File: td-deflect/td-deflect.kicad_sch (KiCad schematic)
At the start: 83 parts, among them J10 Conn_01x02_Male, J11 Conn_01x02_Male, Q1 BSZ42DN25NS3GATMA1, Q10 IPD50R380CE, Q11 IPD50R380CE, Q2 G3R450MT17D, Q3 BSZ42DN25NS3GATMA1, Q4 BCP56, Q5 BCP53, Q6 BD139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

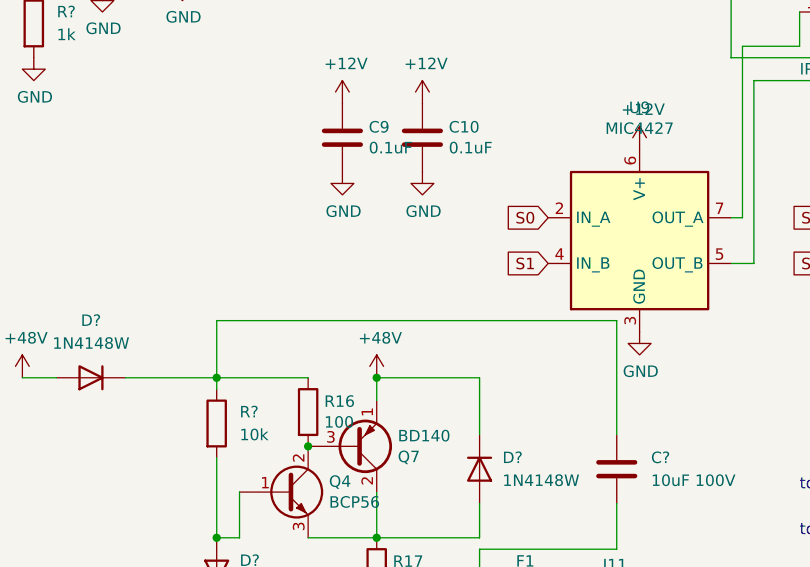
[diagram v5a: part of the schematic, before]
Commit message: make bootstrap circuit not bootstrap as much
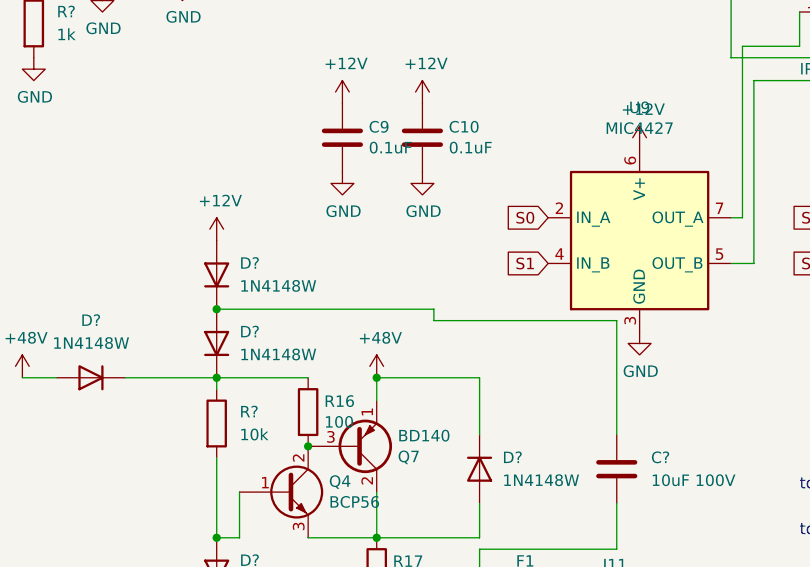
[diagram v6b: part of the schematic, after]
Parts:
- added D? (x2): 1N4148W, Diode_SMD:D_SOD-123, symbol Diode:1N4148W
- C5, C7: Digikey 1276-1099-1-ND -> (none); Voltage 10V -> 50V
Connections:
- net +12V: now also D?.2 (A)
- net at D?.1 (K), R16.1, R?.1: now also D?.1 (K); no longer C?.1
- new net: C?.1, D?.1 (K), D?.2 (A)
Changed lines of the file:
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@@
   (junction (at 214.63 93.98) (diameter 1.016) (color 0 0 0 0)
   )
+  (junction (at 128.27 121.92) (diameter 0) (color 0 0 0 0)
+  )
   (junction (at 71.12 45.72) (diameter 0) (color 0 0 0 0)
   )
@@
     (stroke (width 0) (type default) (color 0 0 0 0))
   )
-  (wire (pts (xy 172.72 123.19) (xy 128.27 123.19))
-    (stroke (width 0) (type default) (color 0 0 0 0))
-  )
   (wire (pts (xy 17.78 166.37) (xy 17.78 168.91))
     (stroke (width 0) (type solid) (color 0 0 0 0))
@@
     (stroke (width 0) (type solid) (color 0 0 0 0))
   )
-  (wire (pts (xy 128.27 123.19) (xy 128.27 129.54))
-    (stroke (width 0) (type default) (color 0 0 0 0))
-  )
   (wire (pts (xy 204.47 93.98) (xy 214.63 93.98))
     (stroke (width 0) (type solid) (color 0 0 0 0))
@@
     (stroke (width 0) (type solid) (color 0 0 0 0))
   )
+  (wire (pts (xy 152.4 123.19) (xy 172.72 123.19))
+    (stroke (width 0) (type default) (color 0 0 0 0))
+  )
   (wire (pts (xy 228.6 83.82) (xy 232.41 83.82))
     (stroke (width 0) (type solid) (color 0 0 0 0))
@@
     (stroke (width 0) (type default) (color 0 0 0 0))
   )
+  (wire (pts (xy 152.4 121.92) (xy 152.4 123.19))
+    (stroke (width 0) (type default) (color 0 0 0 0))
+  )
   (wire (pts (xy 71.12 33.02) (xy 68.58 33.02))
     (stroke (width 0) (type solid) (color 0 0 0 0))
@@
     (stroke (width 0) (type solid) (color 0 0 0 0))
   )
+  (wire (pts (xy 128.27 121.92) (xy 152.4 121.92))
+    (stroke (width 0) (type default) (color 0 0 0 0))
+  )
   (wire (pts (xy 246.38 83.82) (xy 246.38 85.09))
     (stroke (width 0) (type solid) (color 0 0 0 0))
@@
       (effects (font (size 1.27 1.27)) hide)
     )
-    (property "Voltage" "10V" (id 4) (at 77.47 129.54 0)
+    (property "Voltage" "50V" (id 4) (at 77.47 129.54 0)
       (effects (font (size 1.27 1.27)) hide)
     )
-    (property "Digikey" "1276-1099-1-ND" (id 5) (at 77.47 129.54 0)
+    (property "Digikey" "" (id 5) (at 77.47 129.54 0)
       (effects (font (size 1.27 1.27)) hide)
     )
@@
       (effects (font (size 1.27 1.27)) hide)
     )
-    (property "Voltage" "10V" (id 4) (at 90.17 130.81 0)
+    (property "Voltage" "50V" (id 4) (at 90.17 130.81 0)
       (effects (font (size 1.27 1.27)) hide)
     )
-    (property "Digikey" "1276-1099-1-ND" (id 5) (at 90.17 130.81 0)
+    (property "Digikey" "" (id 5) (at 90.17 130.81 0)
       (effects (font (size 1.27 1.27)) hide)
     )
@@
     (pin "4")
   )
+  (symbol (lib_id "power:+12V") (at 128.27 114.3 0) (unit 1)
+    (in_bom yes) (on_board yes)
+    (property "Reference" "#PWR?" (id 0) (at 128.27 118.11 0)
+      (effects (font (size 1.27 1.27)) hide)
+    )
+    (property "Value" "+12V" (id 1) (at 128.651 109.9058 0))
+    (property "Footprint" "" (id 2) (at 128.27 114.3 0)
+      (effects (font (size 1.27 1.27)) hide)
+    )
+    (property "Datasheet" "" (id 3) (at 128.27 114.3 0)
+      (effects (font (size 1.27 1.27)) hide)
+    )
+    (pin "1")
+  )
   (symbol (lib_id "power:GND") (at 107.95 93.98 0) (unit 1)
     (in_bom yes) (on_board yes)
@@
     (pin "2")
   )
+  (symbol (lib_id "Diode:1N4148W") (at 128.27 118.11 90) (unit 1)
+    (in_bom yes) (on_board yes) (fields_autoplaced)
+    (property "Reference" "D?" (id 0) (at 130.81 116.8399 90)
+      (effects (font (size 1.27 1.27)) (justify right))
+    )
+    (property "Value" "1N4148W" (id 1) (at 130.81 119.3799 90)
+      (effects (font (size 1.27 1.27)) (justify right))
+    )
+    (property "Footprint" "Diode_SMD:D_SOD-123" (id 2) (at 132.715 118.11 0)
+      (effects (font (size 1.27 1.27)) hide)
+    )
+    (property "Datasheet" "https://www.vishay.com/docs/85748/1n4148w.pdf" (id 3) (at 128.27 118.11 0)
+      (effects (font (size 1.27 1.27)) hide)
+    )
+    (pin "1")
+    (pin "2")
+  )
   (symbol (lib_id "Diode:1N4148W") (at 157.48 139.7 270) (unit 1)
     (in_bom yes) (on_board yes) (fields_autoplaced)
@@
     (pin "1")
   )
+  (symbol (lib_id "Diode:1N4148W") (at 128.27 125.73 90) (unit 1)
+    (in_bom yes) (on_board yes) (fields_autoplaced)
+    (property "Reference" "D?" (id 0) (at 130.81 124.4599 90)
+      (effects (font (size 1.27 1.27)) (justify right))
+    )
+    (property "Value" "1N4148W" (id 1) (at 130.81 126.9999 90)
+      (effects (font (size 1.27 1.27)) (justify right))
+    )
+    (property "Footprint" "Diode_SMD:D_SOD-123" (id 2) (at 132.715 125.73 0)
+      (effects (font (size 1.27 1.27)) hide)
+    )
+    (property "Datasheet" "https://www.vishay.com/docs/85748/1n4148w.pdf" (id 3) (at 128.27 125.73 0)
+      (effects (font (size 1.27 1.27)) hide)
+    )
+    (pin "1")
+    (pin "2")
+  )
   (symbol (lib_id "Device:R") (at 107.95 90.17 0) (unit 1)
     (in_bom yes) (on_board yes) (fields_autoplaced)
@@
       (reference "#PWR?") (unit 1) (value "-12V") (footprint "")
     )
+    (path "/5b7a1bb3-24df-4abf-84ba-0b9034b3a7c4"
+      (reference "#PWR?") (unit 1) (value "+12V") (footprint "")
+    )
     (path "/00000000-0000-0000-0000-00005d9d9196/5eaa695f-59c3-45de-9623-f11dde8baf91"
       (reference "#PWR?") (unit 1) (value "GND") (footprint "")
@@
       (reference "D?") (unit 1) (value "1N4148W") (footprint "Diode_SMD:D_SOD-123")
     )
+    (path "/9f6b373c-73ae-40b1-af0e-5857c91d4112"
+      (reference "D?") (unit 1) (value "1N4148W") (footprint "Diode_SMD:D_SOD-123")
+    )
     (path "/b5b4e66c-1245-4e6f-b506-9e842e977f02"
       (reference "D?") (unit 1) (value "1N4148W") (footprint "Diode_SMD:D_SOD-123")
     )
+    (path "/d0487f9d-33c5-48db-adad-1d43b0abfe2f"
+      (reference "D?") (unit 1) (value "1N4148W") (footprint "Diode_SMD:D_SOD-123")
+    )

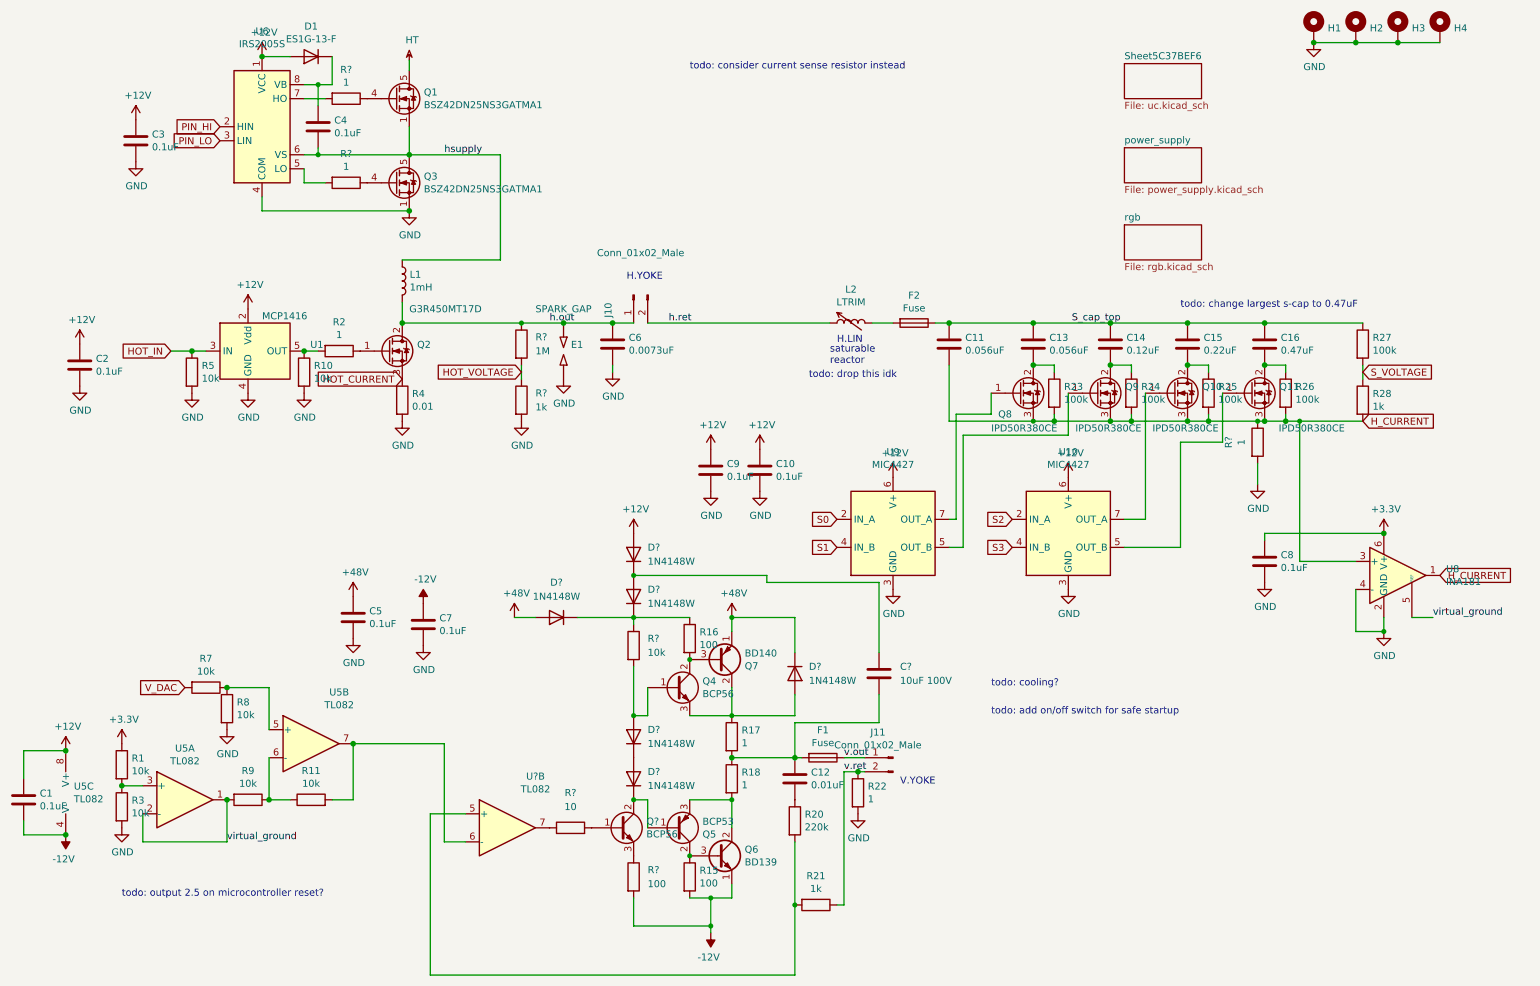
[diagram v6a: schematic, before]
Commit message: add class d vertical amp
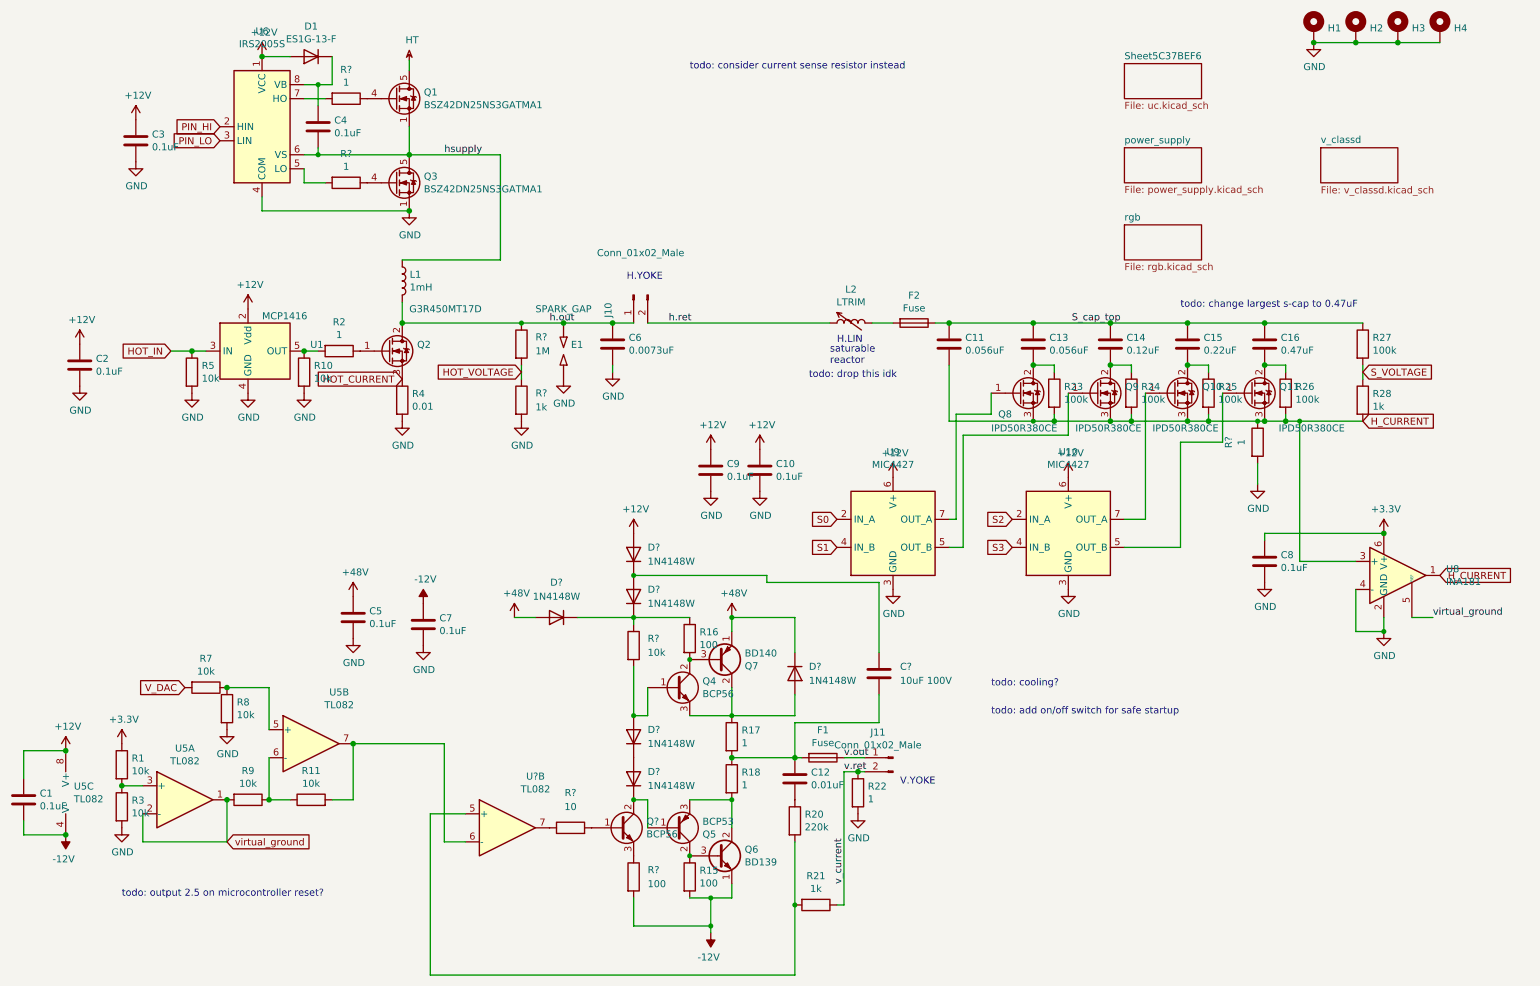
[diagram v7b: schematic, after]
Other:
- added sheet v_classd (v_classd.kicad_sch)

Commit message: switch to smt hot
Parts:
- Q2: value G3R450MT17D -> G3R450MT17J; footprint Package_TO_SOT_THT:TO-247-3_Vertical -> Package_TO_SOT_SMD:TO-263-7_TabPin8; symbol Transistor_FET:C2M0045170D -> Transistor_FET:C3M0280090J; Digikey 1242-G3R450MT17D-ND -> 1242-G3R450MT17J-ND
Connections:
- net GND: now also Q2.2 (DS)
- net HOT_CURRENT: now also Q2.4 (S), Q2.5 (S), Q2.6 (S), Q2.7 (S)
- net h.out: now also Q2.8 (D); no longer Q2.2 (D)
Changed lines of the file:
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@@
   (junction (at 251.46 25.4) (diameter 1.016) (color 0 0 0 0)
   )
+  (junction (at 68.58 88.9) (diameter 0) (color 0 0 0 0)
+  )
   (junction (at 266.7 25.4) (diameter 1.016) (color 0 0 0 0)
   )
@@
   (junction (at 214.63 76.2) (diameter 1.016) (color 0 0 0 0)
   )
+  (junction (at 86.36 86.36) (diameter 0) (color 0 0 0 0)
+  )
   (junction (at 128.27 147.32) (diameter 0) (color 0 0 0 0)
   )
@@
     (stroke (width 0) (type solid) (color 0 0 0 0))
   )
+  (wire (pts (xy 81.28 86.36) (xy 81.28 100.33))
+    (stroke (width 0) (type default) (color 0 0 0 0))
+  )
   (wire (pts (xy 77.47 152.4) (xy 77.47 162.56))
     (stroke (width 0) (type solid) (color 0 0 0 0))
@@
     (stroke (width 0) (type default) (color 0 0 0 0))
   )
+  (wire (pts (xy 81.28 100.33) (xy 77.47 100.33))
+    (stroke (width 0) (type default) (color 0 0 0 0))
+  )
   (wire (pts (xy 87.63 30.48) (xy 87.63 28.575))
     (stroke (width 0) (type solid) (color 0 0 0 0))
@@
     (stroke (width 0) (type solid) (color 0 0 0 0))
   )
+  (wire (pts (xy 86.36 86.36) (xy 81.28 86.36))
+    (stroke (width 0) (type default) (color 0 0 0 0))
+  )
   (wire (pts (xy 142.24 180.34) (xy 146.05 180.34))
     (stroke (width 0) (type solid) (color 0 0 0 0))
@@
     (stroke (width 0) (type default) (color 0 0 0 0))
   )
+  (wire (pts (xy 78.74 83.82) (xy 78.74 88.9))
+    (stroke (width 0) (type default) (color 0 0 0 0))
+  )
   (wire (pts (xy 86.36 64.77) (xy 104.14 64.77))
     (stroke (width 0) (type solid) (color 0 0 0 0))
@@
     (stroke (width 0) (type solid) (color 0 0 0 0))
   )
+  (wire (pts (xy 78.74 88.9) (xy 68.58 88.9))
+    (stroke (width 0) (type default) (color 0 0 0 0))
+  )
   (wire (pts (xy 246.38 93.98) (xy 246.38 92.71))
     (stroke (width 0) (type solid) (color 0 0 0 0))
@@
     )
   )
-  (global_label "HOT_CURRENT" (shape input) (at 86.36 86.36 180) (fields_autoplaced)
+  (global_label "HOT_CURRENT" (shape input) (at 77.47 100.33 180) (fields_autoplaced)
     (effects (font (size 1.27 1.27)) (justify right))
-    (property "Intersheet References" "${INTERSHEET_REFS}" (id 0) (at 0 0 0)
+    (property "Intersheet References" "${INTERSHEET_REFS}" (id 0) (at -8.89 13.97 0)
       (effects (font (size 1.27 1.27)) hide)
     )
@@
     (pin "1")
   )
-  (symbol (lib_id "Transistor_FET:C2M0045170D") (at 83.82 81.28 0) (unit 1)
+  (symbol (lib_id "Transistor_FET:C3M0280090J") (at 83.82 81.28 0) (unit 1)
     (in_bom yes) (on_board yes)
     (property "Reference" "Q2" (id 0) (at 89.0524 80.1116 0)
       (effects (font (size 1.27 1.27)) (justify left))
     )
-    (property "Value" "G3R450MT17D" (id 1) (at 87.63 73.66 0)
+    (property "Value" "G3R450MT17J" (id 1) (at 87.63 73.66 0)
       (effects (font (size 1.27 1.27)) (justify left))
     )
-    (property "Footprint" "Package_TO_SOT_THT:TO-247-3_Vertical" (id 2) (at 83.82 81.28 0)
+    (property "Footprint" "Package_TO_SOT_SMD:TO-263-7_TabPin8" (id 2) (at 83.82 81.28 0)
       (effects (font (size 1.27 1.27) italic) hide)
     )
-    (property "Datasheet" "http://www.genesicsemi.com/sic-mosfet/G3R450MT17D/G3R450MT17D.pdf" (id 3) (at 83.82 81.28 0)
+    (property "Datasheet" "https://genesicsemi.com/sic-mosfet/G3R450MT17J/G3R450MT17J.pdf" (id 3) (at 83.82 81.28 0)
       (effects (font (size 1.27 1.27)) (justify left) hide)
     )
-    (property "Digikey" "1242-G3R450MT17D-ND" (id 4) (at 83.82 81.28 0)
+    (property "Digikey" "1242-G3R450MT17J-ND" (id 4) (at 83.82 81.28 0)
       (effects (font (size 1.27 1.27)) hide)
     )
@@
     (pin "2")
     (pin "3")
+    (pin "4")
+    (pin "5")
+    (pin "6")
+    (pin "7")
+    (pin "8")
   )
   (symbol (lib_id "Device:R") (at 74.93 81.28 270) (unit 1)
@@
     )
     (path "/00000000-0000-0000-0000-00005c36718e"
-      (reference "Q2") (unit 1) (value "G3R450MT17D") (footprint "Package_TO_SOT_THT:TO-247-3_Vertical")
+      (reference "Q2") (unit 1) (value "G3R450MT17J") (footprint "Package_TO_SOT_SMD:TO-263-7_TabPin8")
     )
     (path "/00000000-0000-0000-0000-00005dbc9c3e"
